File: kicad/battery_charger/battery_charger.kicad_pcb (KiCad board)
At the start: 2 copper layers, 54 x 20 mm, 34 parts, among them SW1 SW_Push

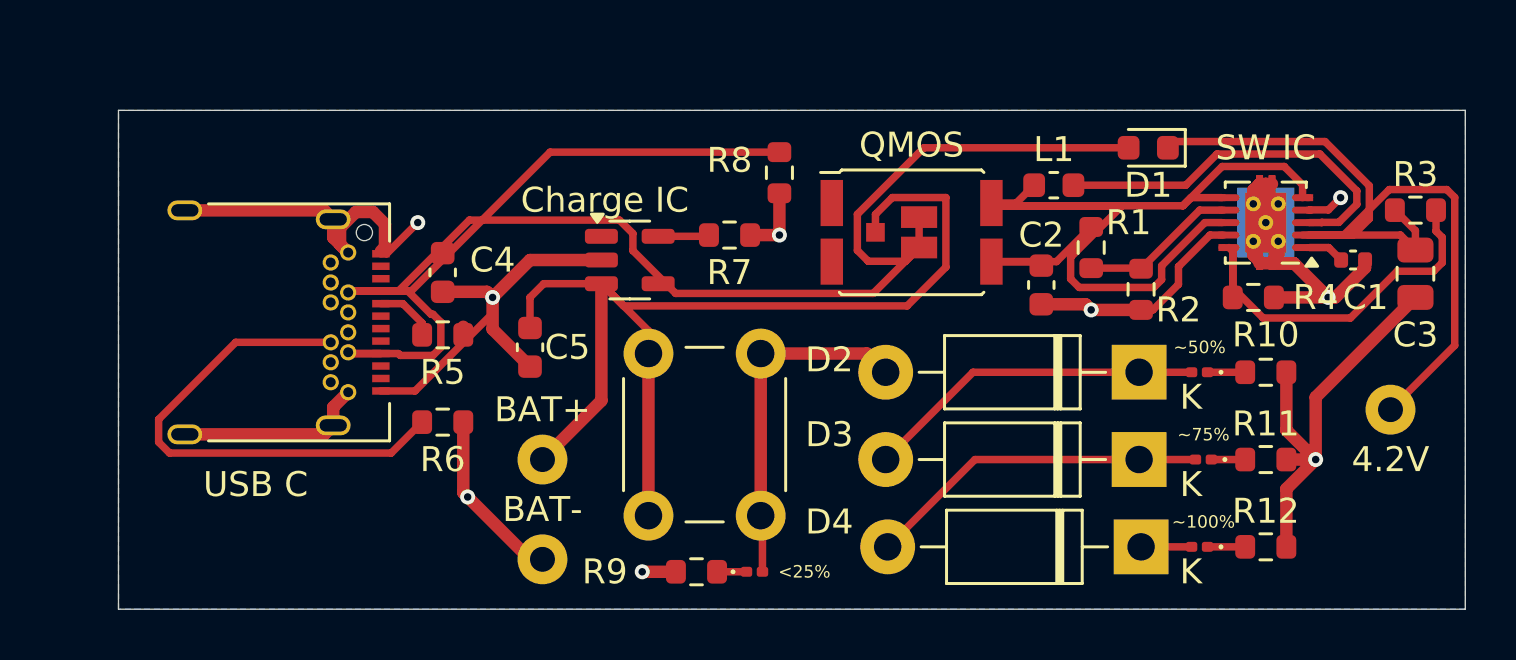
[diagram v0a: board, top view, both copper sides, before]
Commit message: changed to usb b micro, made design longer and thinner
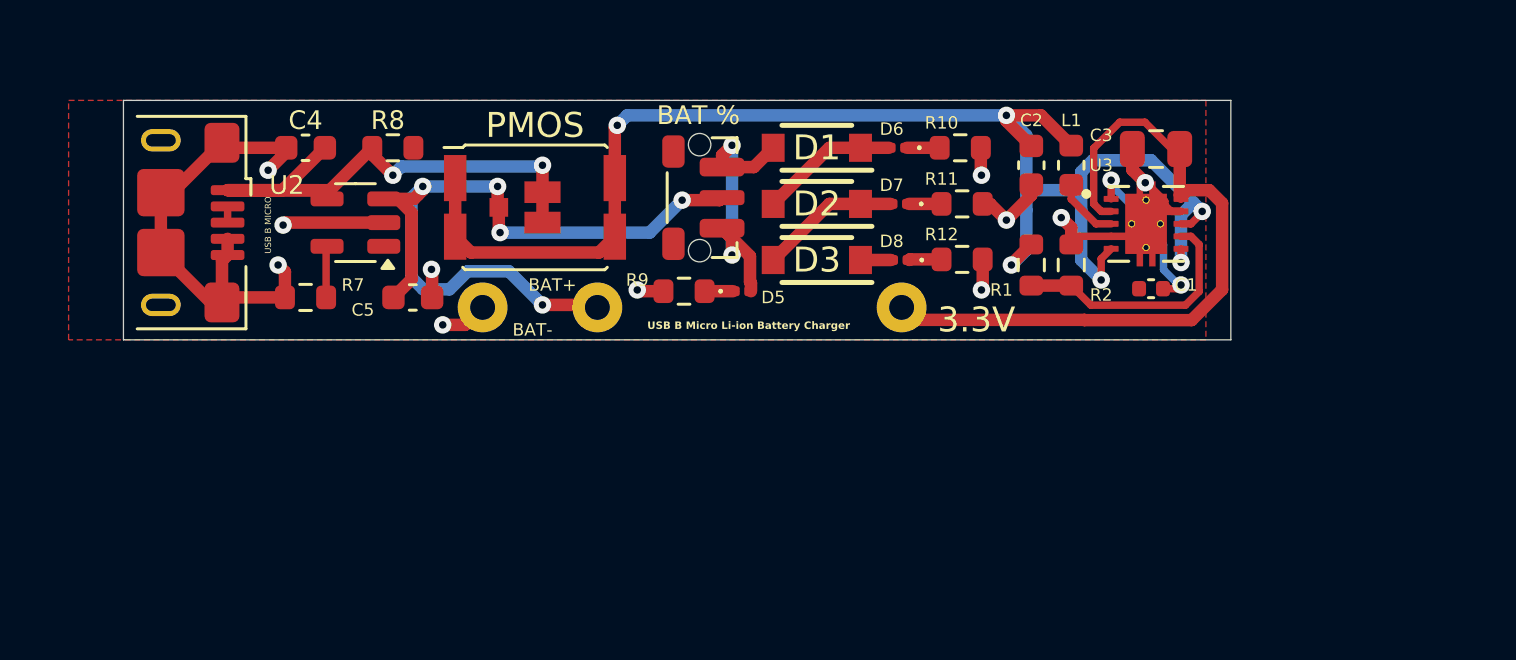
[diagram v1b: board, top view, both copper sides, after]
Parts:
- removed 4.2V: NPTH 1mm, Library:NPTH 1mm
- removed D4: 1N4007, Diode_THT:D_DO-41_SOD81_P10.16mm_Horizontal
- removed R3: 1.48M, Resistor_SMD:R_0603_1608Metric
- removed R4: 200k, Resistor_SMD:R_0603_1608Metric
- removed R5, R6: 5.1k, Resistor_SMD:R_0603_1608Metric
- removed SW IC: TPS61200DRC, Package_SON:Texas_S-PVSON-N10_ThermalVias
- removed USB C: USB_C_Receptacle_USB2.0_16P, Connector_USB:USB_C_Receptacle_Amphenol_12401548E4-2A
- added 3.3V: NPTH 1mm, Library:NPTH 1mm, F.Cu at (139.4, 92.4)
- added U3: TPS61201DRC, Library:TPS61201DRC, F.Cu at (149.2, 85.5)
- added USB B MICRO: USB_B_Micro, Connector_USB:USB_Micro-B_Amphenol_10118193-0001LF_Horizontal, F.Cu at (109.7, 85.5)
- BAT %: renamed from SW1; footprint Button_Switch_THT:SW_PUSH_6mm -> Button_Switch_SMD:SW_Push_1P1T-MP_NO_Horizontal_Alps_SKRTLAE010
- D1: value D_Schottky -> 1N4007; footprint Diode_SMD:D_0603_1608Metric -> Library:SODFL3818X130N
- D2, D3: footprint Diode_THT:D_DO-41_SOD81_P10.16mm_Horizontal -> Library:SODFL3818X130N
- U2: renamed from Charge IC
- moved R7 17.2 mm to (115.5, 88.5), turned to 180 degrees
- moved R12 16.8 mm to (141.8, 87.0)
- moved D8 16.6 mm to (139.3, 87.0)
- moved D7 15.9 mm to (139.3, 84.8)
- moved R11 15.9 mm to (141.8, 84.8)
- moved R8 15.5 mm to (119.0, 82.5), turned to 0 degrees
- moved R10 15.2 mm to (141.8, 82.5)
- moved D3 15.2 mm to (136.0, 87.0)
- moved PMOS 15.1 mm to (124.7, 84.9)
- moved D6 15.1 mm to (139.2, 82.5)
- moved D2 14.6 mm to (136.0, 84.8)
- moved D1 13.3 mm to (136.0, 82.5)
- moved C3 11.5 mm to (149.6, 82.5), turned to 180 degrees
- moved D5 11.3 mm to (133.0, 88.2)
- moved R9 11.3 mm to (130.7, 88.2)
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- renumbered <25% to D5, ~50% to D6, ~75% to D7, ~100% to D8, QMOS to PMOS
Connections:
- BAT % pad 1: Net-(D2-A) -> Net-(D1-A)
- C3 pad 1: 4.2V_OUT -> 3.3V_OUT
- C4 pad 1: Net-(D1-A) -> Net-(J1-VBUS)
- D1 pad 1: 4.2V_OUT -> Net-(D1-K)
- D2 pad 2: Net-(D2-A) -> Net-(D1-K)
- D5 pad 2: Net-(D2-A) -> Net-(D1-A)
- D6 pad 2: Net-(D2-K) -> Net-(D1-K)
- D7 pad 2: Net-(D3-K) -> Net-(D2-K)
- D8 pad 2: Net-(D4-K) -> Net-(D3-K)
- PMOS pad 3: Net-(D1-A) -> Net-(J1-VBUS)
- R8 pad 1: Net-(D1-A) -> Net-(J1-VBUS)
- U2 pad 4: Net-(D1-A) -> Net-(J1-VBUS)
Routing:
- net Net-(D1-A): track 72.6 -> 12.1 mm, vias 0 -> 2
- net GND: track 92.9 -> 43.0 mm, vias 9 -> 11
- net 4.2V_OUT: track 35.9 -> 0.00 mm
- net 3.3V_OUT: track 0.00 -> 28.5 mm
- net Net-(J1-VBUS): track 0.00 -> 25.3 mm, vias 0 -> 2
- net Net-(J1-CC2): track 20.4 -> 0.00 mm
- net Net-(Q1-D): track 40.9 -> 60.4 mm, vias 0 -> 6
- net Net-(U1-FB): track 15.6 -> 0.00 mm
- net Net-(D2-A): track 14.1 -> 0.00 mm
- net Net-(U3-L): track 15.2 -> 2.58 mm
- net Net-(D3-K): track 13.8 -> 1.24 mm
- net Net-(Q1-S): track 43.9 -> 33.7 mm, vias 0 -> 5
- net Net-(D2-K): track 13.7 -> 5.65 mm
- net Net-(D1-K): track 0.00 -> 5.57 mm
- net Net-(U3-VAUX): track 1.47 -> 6.94 mm, vias 0 -> 2
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- added copper zone on F.Cu, net GND
- removed copper zone on B.Cu, net GND
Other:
- board size 54 x 20 mm -> 44.4 x 9.6 mm
- board text added: "USB B Micro Li-ion Battery Charger"

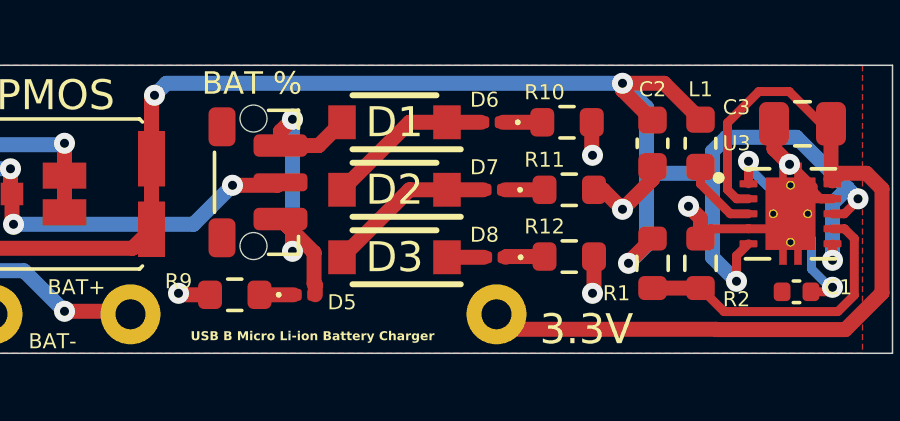
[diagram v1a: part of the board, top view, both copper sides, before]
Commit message: labeled LED battery % display
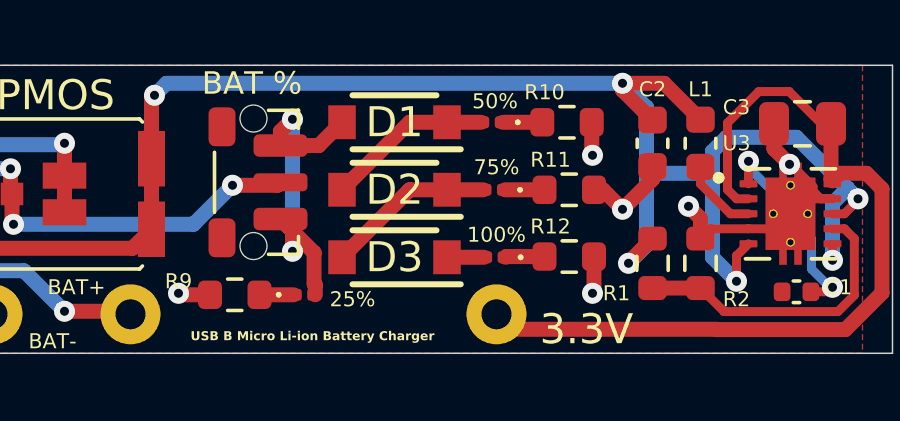
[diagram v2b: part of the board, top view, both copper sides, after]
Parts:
- renumbered D8 to 100%, D5 to 25%, D6 to 50%, D7 to 75%
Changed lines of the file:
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@@
 		(tags "resistor")
 		(property "Reference" "R11"
-			(at -0.825 -1 0)
+			(at -0.625 -1 0)
 			(layer "F.SilkS")
 			(effects
@@
 		(tags "resistor")
 		(property "Reference" "R12"
-			(at -0.825 -1 0)
+			(at -0.625 -1 0)
 			(layer "F.SilkS")
 			(effects
@@
 		(descr "LED SMD 0201 (0603 Metric), square (rectangular) end terminal, IPC_7351 nominal, (Body size source: https://www.vishay.com/docs/20052/crcw0201e3.pdf), generated with kicad-footprint-generator")
 		(tags "LED")
-		(property "Reference" "D8"
-			(at 0.345 0.75 0)
+		(property "Reference" "100%"
+			(at -0.055 0.75 0)
 			(layer "F.SilkS")
 			(effects
@@
 		(descr "LED SMD 0201 (0603 Metric), square (rectangular) end terminal, IPC_7351 nominal, (Body size source: https://www.vishay.com/docs/20052/crcw0201e3.pdf), generated with kicad-footprint-generator")
 		(tags "LED")
-		(property "Reference" "D6"
-			(at 0.25 0.75 0)
+		(property "Reference" "50%"
+			(at -0.1 0.7 0)
 			(layer "F.SilkS")
 			(effects
@@
 		(descr "LED SMD 0201 (0603 Metric), square (rectangular) end terminal, IPC_7351 nominal, (Body size source: https://www.vishay.com/docs/20052/crcw0201e3.pdf), generated with kicad-footprint-generator")
 		(tags "LED")
-		(property "Reference" "D5"
-			(at 1.25 0.25 0)
+		(property "Reference" "25%"
+			(at 1.6 0.15 0)
 			(layer "F.SilkS")
 			(effects
@@
 		(descr "LED SMD 0201 (0603 Metric), square (rectangular) end terminal, IPC_7351 nominal, (Body size source: https://www.vishay.com/docs/20052/crcw0201e3.pdf), generated with kicad-footprint-generator")
 		(tags "LED")
-		(property "Reference" "D7"
-			(at 0.325 0.75 0)
+		(property "Reference" "75%"
+			(at -0.075 0.75 0)
 			(layer "F.SilkS")
 			(effects

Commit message: neues aus dem labor
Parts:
- removed PMOS: Q_PMOS_DSG, Package_DirectFET:DirectFET_MX
- added GND: NPTH 1mm, Library:NPTH 1mm, F.Cu at (134.8, 92.4)
- added Q1: Q_PMOS_GSD, Package_TO_SOT_SMD:SOT-23-3, F.Cu at (122.3, 85.2)
- added REF**: jlcpcb_tooling_hole, Library:jlcpcb_tooling_hole, F.Cu at (147.2, 91.2)
- added REF**: jlcpcb_tooling_hole, Library:jlcpcb_tooling_hole, F.Cu at (147.2, 79.6)
- added REF**: jlcpcb_tooling_hole, Library:jlcpcb_tooling_hole, F.Cu at (113.2, 79.6)
- D1, D2, D3: footprint Library:SODFL3818X130N -> Diode_SMD:D_SOD-123F
- D5: renamed from 25%; footprint LED_SMD:LED_0201_0603Metric -> LED_SMD:LED_0402_1005Metric
- D6: renamed from 50%; footprint LED_SMD:LED_0201_0603Metric -> LED_SMD:LED_0402_1005Metric
- D7: renamed from 75%; footprint LED_SMD:LED_0201_0603Metric -> LED_SMD:LED_0402_1005Metric
- D8: renamed from 100%; footprint LED_SMD:LED_0201_0603Metric -> LED_SMD:LED_0402_1005Metric
- J1: renamed from USB B MICRO
- SW1: renamed from BAT %; footprint Button_Switch_SMD:SW_Push_1P1T-MP_NO_Horizontal_Alps_SKRTLAE010 -> Button_Switch_SMD:SW_SPST_B3U-1000P
- moved B+ 8.24 mm to (122.7, 85.5)
- moved D1 4.43 mm to (131.6, 81.9)
- moved D2 4.42 mm to (131.6, 84.2)
- moved D3 4.41 mm to (131.6, 86.6)
- moved R12 4.39 mm to (137.4, 86.9)
- moved R9 4.39 mm to (126.3, 88.2)
- moved SW1 4.39 mm to (126.9, 84.5)
- moved C1 4.39 mm to (145.0, 88.2)
- moved C2 4.39 mm to (140.2, 83.2)
- moved C3 4.39 mm to (145.2, 82.5)
- moved D6 4.39 mm to (134.9, 82.5)
- moved D7 4.39 mm to (134.9, 84.8)
- moved D8 4.39 mm to (135.0, 87.0)
- moved L1 4.39 mm to (141.8, 83.2)
- moved R1 4.39 mm to (140.2, 87.2)
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- renumbered BAT+ to B+, BAT- to B-
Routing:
- net Net-(Q1-S): track 33.7 -> 16.6 mm, vias 5 -> 0
- net Net-(Q1-D): track 60.4 -> 48.8 mm
- net Net-(J1-VBUS): track 25.3 -> 19.3 mm, vias 2 -> 0
- net 3.3V_OUT: track 28.5 -> 25.3 mm
- net Net-(D1-A): track 12.1 -> 10.2 mm, vias 2 -> 0
- added copper zone on B.Cu, net GND
- removed copper zone on F.Cu, net GND
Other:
- board size 44.4 x 9.6 mm -> 40 x 13.6 mm
- board text removed: "USB B Micro Li-ion Battery Charger"
